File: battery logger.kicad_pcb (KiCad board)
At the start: 2 copper layers, 47 parts, among them CON501 BARREL_JACK, IC301 ATMEGA328-P, P201 CONN_01X02, P202 CONN_01X03, P301 CONN_02X03, P302 CONN_01X05, P501 CONN_01X02, P601 CONN_01X04, Q201 BUK9575, SW301 SW_PUSH, U201 TS922, U401 TLC2274, U501 LM2931ADT-5.0, U601 74HC14, X301 CRYSTAL 16MHZ

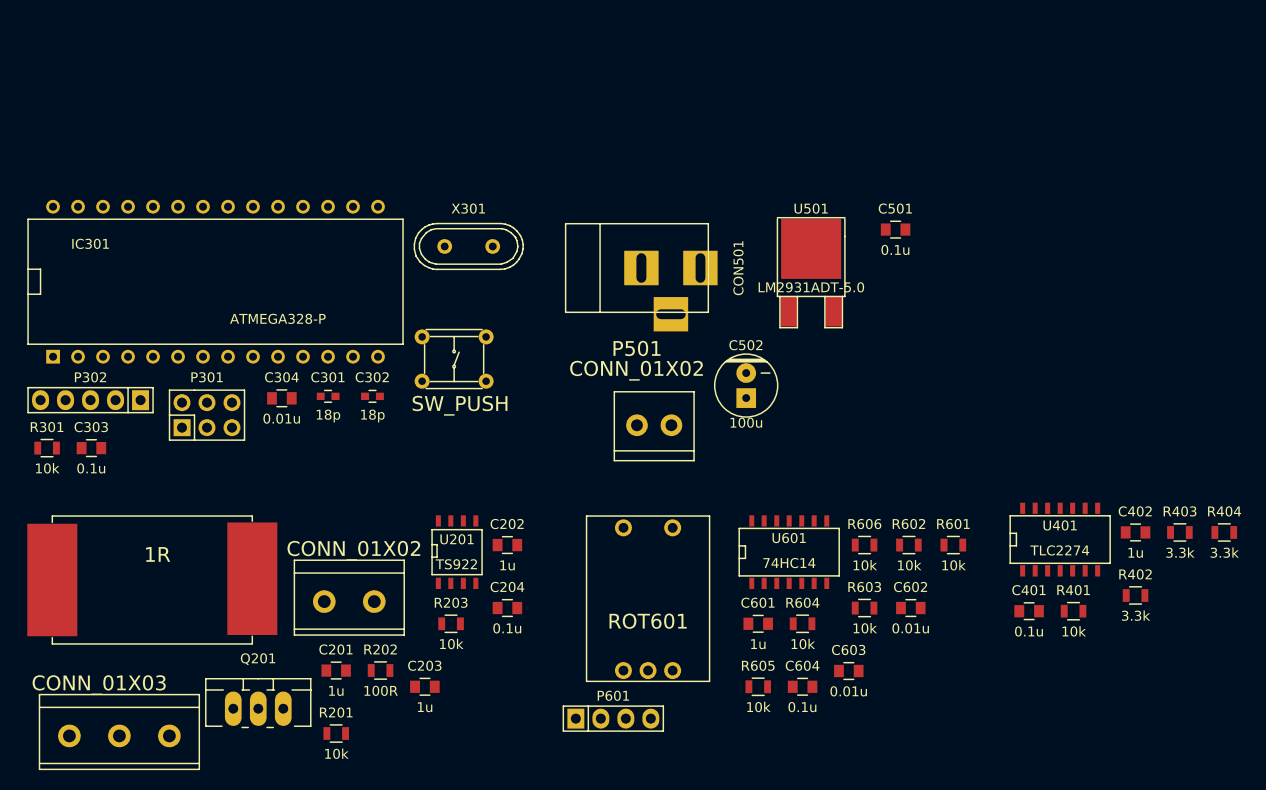
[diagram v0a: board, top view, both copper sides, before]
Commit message: initial part placemen
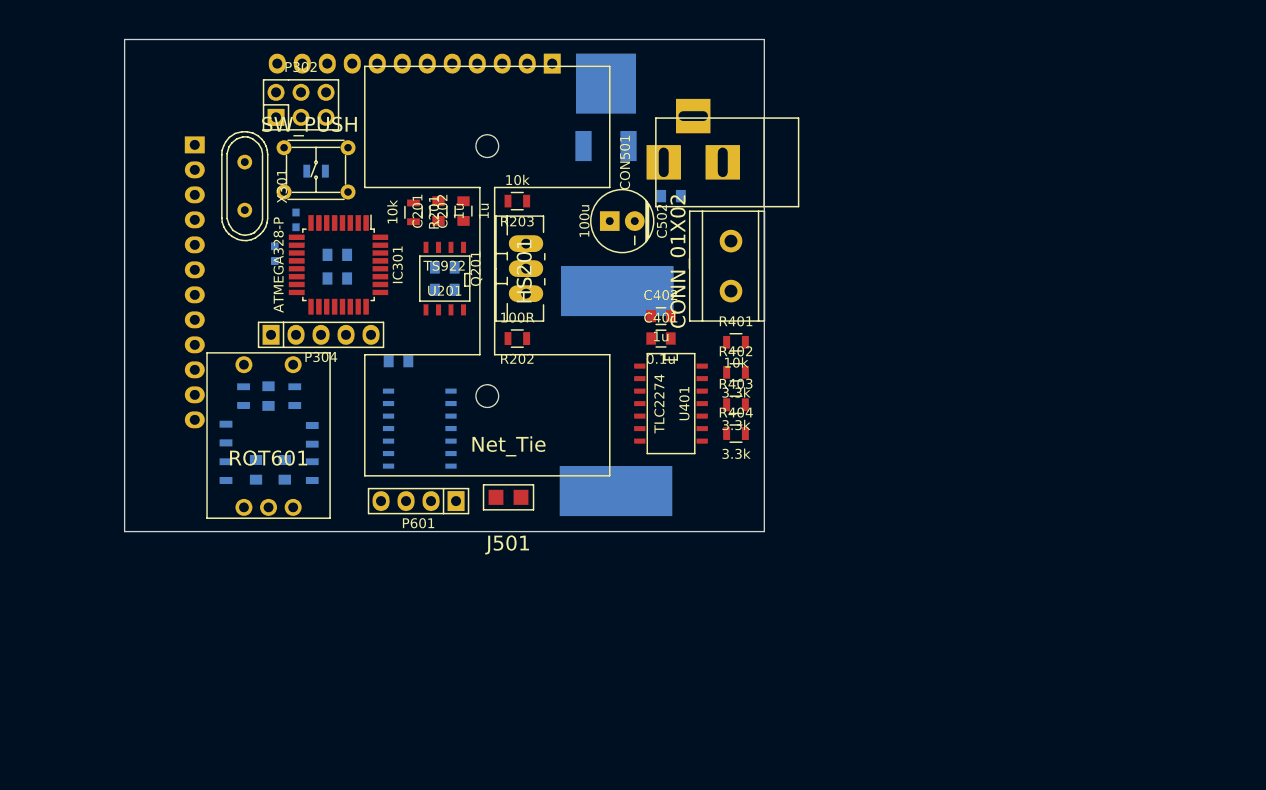
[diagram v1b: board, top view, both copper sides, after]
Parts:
- removed P202: CONN_01X03, battery logger:Terminal_Block_1x3_5.08mm
- removed P501: CONN_01X02, battery logger:Terminal_Block_1x2_3.5mm
- added HS201: HEATSINK, battery logger:FA-T220-38E, F.Cu at (196.8, 73.5)
- added J501: Net_Tie, battery logger:Net_Tie, F.Cu at (199.0, 96.5)
- added P303: CONN_01X12, Pin_Headers:Pin_Header_Straight_1x12, B.Cu at (189.5, 52.5)
- added P304: CONN_01X05, Socket_Strips:Socket_Strip_Straight_1x05, F.Cu at (180.0, 80.0)
- C203, C204, C301, C302, C303, C304, C501, C601, C602, C603, C604, R204, R301, R601, R602, R603, R604, R605, R606, U501, U601: moved to B.Cu
- IC301: footprint Sockets_DIP:DIP-28__600 -> Housings_QFP:TQFP-32_7x7mm_Pitch0.8mm
- P301: value CONN_02X03 -> CONN_01X12; footprint Pin_Headers:Pin_Header_Straight_2x03 -> Pin_Headers:Pin_Header_Straight_1x12; moved to B.Cu
- P302: value CONN_01X05 -> CONN_02X03; footprint Socket_Strips:Socket_Strip_Straight_1x05 -> Pin_Headers:Pin_Header_Straight_2x03
- moved R602 69.3 mm to (172.1, 86.2), turned to 270 degrees
- moved R601 68.6 mm to (177.3, 86.2), turned to 90 degrees
- moved R606 65.9 mm to (170.3, 90.0), turned to 270 degrees
- moved C602 65.1 mm to (176.3, 93.7), turned to 270 degrees
- moved R204 64.5 mm to (210.1, 75.6), turned to 270 degrees
- moved C603 63.6 mm to (173.4, 93.7), turned to 270 degrees
- moved R605 58.3 mm to (170.3, 93.9), turned to 90 degrees
- moved R603 57.8 mm to (179.1, 93.9), turned to 270 degrees
- moved C601 54.9 mm to (174.6, 86.2), turned to 90 degrees
- moved R201 53.5 mm to (189.4, 67.6), turned to 270 degrees
- moved R604 53.4 mm to (179.1, 90.2), turned to 270 degrees
- moved C402 53.0 mm to (214.5, 78.1)
- moved C604 52.7 mm to (187.8, 82.7)
- moved Q201 52.3 mm to (200.8, 73.3), turned to 90 degrees
- moved P201 52.0 mm to (221.6, 75.6), turned to 90 degrees
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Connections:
- C203 pad 1: /Current Sink/Enable -> /Current Sink/ENABLE
- C204 pad 1: /Current Sink/Enable -> /Current Sink/ENABLE
- IC301 pad 14: /Current Sink/Enable -> /Current Sink/ENABLE
- IC301 pad 4: /Encoder Interface/ENC_BTN -> /Encoder Interface/ENC_SW
- P301 pad 1: /uController/PB4 -> /uController/PC6
- P301 pad 2: VCC -> /uController/PD0
- P301 pad 3: /uController/CLK -> /uController/PD1
- P301 pad 4: /uController/DAT -> /Encoder Interface/ENC_SW
- P301 pad 5: /uController/PC6 -> /uController/PD3
- P301 pad 6: GNDD -> /Encoder Interface/ENC_A
- P302 pad 1: /uController/LAT -> /uController/PB4
- P302 pad 2: /uController/DAT -> VCC
- P302 pad 4: VCC -> /uController/DAT
- P302 pad 5: GNDD -> /uController/PC6
- P601 pad 3: /Encoder Interface/EMC_B -> /Encoder Interface/ENC_B
- U201 pad 8: /Current Sink/Enable -> /Current Sink/ENABLE
- U601 pad 12: /Encoder Interface/ENC_B -> /Encoder Interface/ENC_SW
- U601 pad 13: Net-(C603-Pad1) -> Net-(C601-Pad1)
- U601 pad 8: /Encoder Interface/ENC_BTN -> /Encoder Interface/ENC_B
- U601 pad 9: Net-(C601-Pad1) -> Net-(C603-Pad1)
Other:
- board outline added: 65 x 50 mm

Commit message: tweaking part layout
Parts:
- removed P601: CONN_01X04, Pin_Headers:Pin_Header_Straight_1x04
- added M3 screw hole: VAL**, battery logger:M3_screw_hole, F.Cu at (222.0, 52.6)
- added M3 screw hole: VAL**, battery logger:M3_screw_hole, F.Cu at (222.0, 97.4)
- added M3 screw hole: VAL**, battery logger:M3_screw_hole, F.Cu at (166.5, 97.4)
- added M3 screw hole: VAL**, battery logger:M3_screw_hole, F.Cu at (167.3, 52.6)
- added P305: CONN_01X01, Pin_Headers:Pin_Header_Straight_1x01, B.Cu at (197.4, 52.3)
- added P306: CONN_01X01, Pin_Headers:Pin_Header_Straight_1x01, B.Cu at (193.8, 52.3)
- added P307: CONN_01X01, Pin_Headers:Pin_Header_Straight_1x01, B.Cu at (190.2, 52.3)
- added P308: CONN_01X01, Pin_Headers:Pin_Header_Straight_1x01, B.Cu at (186.7, 52.3)
- added P309: CONN_01X01, Pin_Headers:Pin_Header_Straight_1x01, B.Cu at (189.1, 81.4)
- added P310: CONN_01X01, Pin_Headers:Pin_Header_Straight_1x01, B.Cu at (192.5, 81.4)
- added P311: CONN_01X01, Pin_Headers:Pin_Header_Straight_1x01, B.Cu at (196.1, 81.4)
- added P312: CONN_01X05, Socket_Strips:Socket_Strip_Straight_1x05, F.Cu at (171.8, 70.2)
- C401, C402: moved to B.Cu
- HS201: footprint battery logger:FA-T220-38E -> battery logger:FA-TO220-64E
- P301: value CONN_01X12 -> CONN_01X09; footprint Pin_Headers:Pin_Header_Straight_1x12 -> Pin_Headers:Pin_Header_Straight_1x09
- P303: value CONN_01X12 -> CONN_01X01; footprint Pin_Headers:Pin_Header_Straight_1x12 -> Pin_Headers:Pin_Header_Straight_1x01
- P304: value CONN_01X05 -> CONN_01X01; footprint Socket_Strips:Socket_Strip_Straight_1x05 -> Pin_Headers:Pin_Header_Straight_1x01; moved to B.Cu
- moved J501 39.8 mm to (198.9, 56.8)
- moved P304 34.7 mm to (200.9, 52.3), turned to 270 degrees
- moved P303 14.9 mm to (204.3, 52.3), turned to 90 degrees
- moved C402 9.65 mm to (209.3, 86.2), turned to 270 degrees
- moved P301 6.93 mm to (168.1, 67.8), turned to 180 degrees
- moved C401 6.48 mm to (211.7, 86.2), turned to 270 degrees
- moved X301 6.38 mm to (175.9, 70.1)
- moved R404 5.62 mm to (216.8, 91.8), turned to 180 degrees
- moved C302 5.03 mm to (180.2, 70.9), turned to 0 degrees
- moved U501 4.35 mm to (208.4, 65.2)
- moved P302 3.81 mm to (179.8, 53.3)
- moved C502 3.66 mm to (213.6, 70.5)
- moved R202 3.25 mm to (202.7, 82.0)
- moved R203 3.14 mm to (202.6, 68.1)
- moved C303 2.87 mm to (184.4, 73.7)
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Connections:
- P301 pad 4: /Encoder Interface/ENC_SW -> /uController/PD3
- P301 pad 5: /uController/PD3 -> /uController/PB6
- P301 pad 6: /Encoder Interface/ENC_A -> /uController/PB7
- P301 pad 7: /uController/PB6 -> /uController/PD6
- P301 pad 8: /uController/PB7 -> /uController/PD7
- P301 pad 9: /Encoder Interface/ENC_B -> /Current Sink/ENABLE
- P304 pad 1: /uController/LAT -> /Current Sink/I_SNS
- U601 pad 12: /Encoder Interface/ENC_SW -> /Encoder Interface/ENC_B
- U601 pad 13: Net-(C601-Pad1) -> Net-(C603-Pad1)
- U601 pad 8: /Encoder Interface/ENC_B -> /Encoder Interface/ENC_SW
- U601 pad 9: Net-(C603-Pad1) -> Net-(C601-Pad1)
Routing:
- net /Current Sink/BATT_V: track 0.00 -> 21.0 mm
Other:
- board size 65 x 50 mm -> 65 x 50.8 mm

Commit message: finished layout
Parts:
- removed C603: 0.01u, Capacitors_SMD:C_0805
- removed C604: 0.1u, Capacitors_SMD:C_0805
- removed CON501: BARREL_JACK, Connect:BARREL_JACK
- removed J501: Net_Tie, battery logger:Net_Tie
- removed the M3 screw hole at (222.0, 52.6)
- removed the M3 screw hole at (222.0, 97.4)
- removed the M3 screw hole at (166.5, 97.4)
- removed the M3 screw hole at (167.3, 52.6)
- removed P306, P307, P308, P309, P310, P311: CONN_01X01, Pin_Headers:Pin_Header_Straight_1x01
- removed P312: CONN_01X05, Socket_Strips:Socket_Strip_Straight_1x05
- removed R601, R602, R603, R604, R605, R606: 10k, Resistors_SMD:R_0805
- removed ROT601: Rotary_Encoder, battery logger:PEC11R
- added C503: 0.01u, Capacitors_SMD:C_0805, B.Cu at (173.4, 94.4)
- added C504: 0.1u, Capacitors_SMD:C_0805, B.Cu at (185.3, 80.5)
- added CON601: BARREL_JACK, Connect:BARREL_JACK, F.Cu at (221.5, 61.3)
- added D201: DIODESCH, Diodes_SMD:Diode-SMB_Standard, F.Cu at (212.4, 76.1)
- added F601: FUSE, battery logger:PTC_1206, B.Cu at (214.6, 65.9)
- added J601: Net_Tie, battery logger:Net_Tie2, B.Cu at (190.8, 59.1)
- added M3 screw hole: VAL**, battery logger:M3_screw_hole, F.Cu at (222.0, 97.4)
- added M3 screw hole: VAL**, battery logger:M3_screw_hole, F.Cu at (183.8, 97.3)
- added M3 screw hole: VAL**, battery logger:M3_screw_hole, F.Cu at (171.1, 52.7)
- added M3 screw hole: VAL**, battery logger:M3_screw_hole, F.Cu at (221.9, 52.7)
- added P202: CONN_02X02, Pin_Headers:Pin_Header_Straight_2x02, F.Cu at (219.7, 79.5)
- added P601: CONN_01X02, Pin_Headers:Pin_Header_Straight_1x02, F.Cu at (214.9, 52.2)
- added R205: 10k, Resistors_SMD:R_0805, F.Cu at (196.1, 69.2)
- added R501: 10k, Resistors_SMD:R_0805, B.Cu at (177.6, 86.9)
- added R502: 10k, Resistors_SMD:R_0805, B.Cu at (171.8, 86.9)
- added R503: 10k, Resistors_SMD:R_0805, B.Cu at (179.4, 94.5)
- added R504: 10k, Resistors_SMD:R_0805, B.Cu at (179.4, 90.7)
- added R505: 10k, Resistors_SMD:R_0805, B.Cu at (170.3, 94.5)
- added R506: 10k, Resistors_SMD:R_0805, B.Cu at (170.3, 90.6)
- added ROT501: Rotary_Encoder, battery logger:PEC11R, F.Cu at (174.7, 90.7)
- added TH201: THERMISTOR, battery logger:SolderWirePad_2x_0-8mmDrill, F.Cu at (202.5, 68.0)
- C501: value 0.1u -> 1u
- C502: value 100u -> 0.01u; footprint battery logger:Capacitor6.4x6RM2.5 -> Capacitors_SMD:C_0805; moved to B.Cu
- C601: value 1u -> 0.1u
- C602: value 0.01u -> 100u; footprint Capacitors_SMD:C_0805 -> battery logger:Capacitor6.4x6RM2.5; moved to F.Cu
- IC301: value ATMEGA328-P -> ATMEGA328P-A
- P301: value CONN_01X09 -> CONN_02X03; footprint Pin_Headers:Pin_Header_Straight_1x09 -> Pin_Headers:Pin_Header_Straight_2x03; moved to F.Cu
- P303, P305: value CONN_01X01 -> CONN_01X07; footprint Pin_Headers:Pin_Header_Straight_1x01 -> Pin_Headers:Pin_Header_Straight_1x07; moved to F.Cu
- P304: value CONN_01X01 -> CONN_02X02; footprint Pin_Headers:Pin_Header_Straight_1x01 -> Pin_Headers:Pin_Header_Straight_2x02; moved to F.Cu
- R204: footprint battery logger:FA -> battery logger:8035_J-Lead
- SW301: value SW_PUSH -> SW_PUSH_4_PIN
- U501: value LM2931ADT-5.0 -> 74HC14; footprint SMD_Packages:DPAK-2 -> SMD_Packages:SOIC-14_N
- U601: value 74HC14 -> LM2931ADT-5.0; footprint SMD_Packages:SOIC-14_N -> SMD_Packages:DPAK-2
- moved P305 46.7 mm to (204.4, 98.5), turned to 270 degrees
- moved C501 44.8 mm to (174.8, 86.9), turned to 90 degrees
- moved C502 44.2 mm to (176.5, 94.4)
- moved C602 42.0 mm to (212.3, 70.1)
- moved C601 39.3 mm to (209.8, 66.0), turned to 180 degrees
- moved P304 34.9 mm to (170.6, 69.5), turned to 90 degrees
- moved U601 34.6 mm to (208.4, 61.7), turned to 180 degrees
- moved U501 31.0 mm to (188.3, 88.7), turned to 270 degrees
- moved P302 24.2 mm to (171.9, 76.2), turned to 270 degrees
- moved P303 17.5 mm to (186.9, 52.2)
- moved P301 16.3 mm to (177.8, 54.7), turned to 90 degrees
- moved R201 13.3 mm to (187.1, 81.2), turned to 0 degrees
- moved C201 12.6 mm to (195.0, 81.3), turned to 270 degrees
- moved C202 12.3 mm to (190.5, 79.3), turned to 270 degrees
- moved R403 11.5 mm to (214.9, 97.3)
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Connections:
- C201 pad 2: GND -> GNDD
- C501 pad 2: GND -> GNDD
- C502 pad 1: VCC -> Net-(C502-Pad1)
- C502 pad 2: GND -> GNDD
- C602 pad 1: Net-(C602-Pad1) -> VCC
- IC301 pad 1: /uController/PC6 -> /Current Sink/ENABLE
- IC301 pad 10: /uController/PB7 -> /uController/PD6
- IC301 pad 11: /Encoder Interface/ENC_B -> /uController/PD7
- IC301 pad 12: /uController/PD6 -> /uController/PB0
- IC301 pad 13: /uController/PD7 -> /Current Sink/V_SET
- IC301 pad 14: /Current Sink/ENABLE -> /uController/LAT
- IC301 pad 15: /Current Sink/V_SET -> /uController/DAT
- IC301 pad 16: /uController/LAT -> /uController/MISO
- IC301 pad 17: /uController/DAT -> /uController/CLK
- IC301 pad 18: /uController/PB4 -> VCC
- IC301 pad 19: /uController/CLK -> /uController/ADC6
- IC301 pad 2: /uController/PD0 -> /Encoder Interface/ENC_A
- IC301 pad 20: VCC -> /uController/AREF
- IC301 pad 21: /uController/AREF -> GNDD
- IC301 pad 22: GNDD -> /uController/ADC7
- IC301 pad 23: /Input Voltage Range Switch/V_SNS1 -> /Input Voltage Range Switch/V_SNS4
- IC301 pad 24: /Input Voltage Range Switch/V_SNS2 -> /Input Voltage Range Switch/V_SNS3
- IC301 pad 25: /Input Voltage Range Switch/V_SNS3 -> /Input Voltage Range Switch/V_SNS2
- IC301 pad 26: /Input Voltage Range Switch/V_SNS4 -> /Input Voltage Range Switch/V_SNS1
- IC301 pad 28: /uController/PC5 -> /Current Sink/AUX
- IC301 pad 29: (no net) -> /uController/PC6
- IC301 pad 3: /uController/PD1 -> GNDD
- IC301 pad 30: (no net) -> /uController/PD0
- IC301 pad 31: (no net) -> /uController/PD1
- IC301 pad 32: (no net) -> /Encoder Interface/ENC_SW
- IC301 pad 4: /Encoder Interface/ENC_SW -> VCC
- IC301 pad 5: /uController/PD3 -> GNDD
- IC301 pad 6: /Encoder Interface/ENC_A -> VCC
- IC301 pad 7: VCC -> /uController/PB6
- IC301 pad 8: GNDD -> /uController/PB7
- IC301 pad 9: /uController/PB6 -> /Encoder Interface/ENC_B
- P201 pad 1: /Current Sink/BATT_V -> Net-(D201-Pad1)
- P301 pad 1: /uController/PC6 -> /uController/MISO
- P301 pad 2: /uController/PD0 -> VCC
- P301 pad 3: /uController/PD1 -> /uController/CLK
- P301 pad 4: /uController/PD3 -> /uController/DAT
- P301 pad 5: /uController/PB6 -> /uController/PC6
- P301 pad 6: /uController/PB7 -> GNDD
- P302 pad 1: /uController/PB4 -> VCC
- P302 pad 2: VCC -> /uController/LAT
- P302 pad 3: /uController/CLK -> GNDD
- P302 pad 5: /uController/PC6 -> GNDD
- P302 pad 6: GNDD -> /uController/CLK
- P303 pad 1: /uController/PC5 -> /uController/PD1
- P304 pad 1: /Current Sink/I_SNS -> /Current Sink/V_SET
- P305 pad 1: /Input Voltage Range Switch/V_SNS4 -> /Input Voltage Range Switch/V_SNS1
- Q201 pad D: /Current Sink/BATT_V -> Net-(D201-Pad2)
- SW301 pad 1: GND -> /uController/PC6
- SW301 pad 2: /uController/PC6 -> GNDD
- SW301 pad 3: (no net) -> GNDD
- SW301 pad 4: (no net) -> /uController/PC6
- U201 pad 5: (no net) -> Net-(R205-Pad2)
- U201 pad 6: (no net) -> /Current Sink/AUX
- U201 pad 7: (no net) -> /Current Sink/AUX
- U401 pad 1: /Input Voltage Range Switch/V_SNS1 -> /Input Voltage Range Switch/V_SNS4
- U401 pad 10: Net-(R402-Pad2) -> Net-(R401-Pad2)
- U401 pad 12: Net-(R403-Pad2) -> /Current Sink/BATT_V
- U401 pad 13: /Input Voltage Range Switch/V_SNS4 -> /Input Voltage Range Switch/V_SNS1
- U401 pad 14: /Input Voltage Range Switch/V_SNS4 -> /Input Voltage Range Switch/V_SNS1
- U401 pad 2: /Input Voltage Range Switch/V_SNS1 -> /Input Voltage Range Switch/V_SNS4
- U401 pad 3: /Current Sink/BATT_V -> Net-(R403-Pad2)
- U401 pad 5: Net-(R401-Pad2) -> Net-(R402-Pad2)
- U401 pad 6: /Input Voltage Range Switch/V_SNS2 -> /Input Voltage Range Switch/V_SNS3
- U401 pad 7: /Input Voltage Range Switch/V_SNS2 -> /Input Voltage Range Switch/V_SNS3
- U401 pad 8: /Input Voltage Range Switch/V_SNS3 -> /Input Voltage Range Switch/V_SNS2
- U401 pad 9: /Input Voltage Range Switch/V_SNS3 -> /Input Voltage Range Switch/V_SNS2
- U501 pad 1: Net-(C501-Pad1) -> Net-(U501-Pad1)
- U501 pad 2: GND -> Net-(U501-Pad2)
- U501 pad 3: VCC -> Net-(U501-Pad3)
- U601 pad 1: Net-(U601-Pad1) -> Net-(C601-Pad1)
- U601 pad 2: Net-(U601-Pad2) -> GND
- U601 pad 3: Net-(U601-Pad3) -> VCC
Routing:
- net VCC: track 0.00 -> 241.8 mm, vias 0 -> 8
- net /Input Voltage Range Switch/V_SNS2: track 0.00 -> 64.6 mm, vias 0 -> 4
- net /Input Voltage Range Switch/V_SNS3: track 0.00 -> 64.5 mm, vias 0 -> 4
- net /Input Voltage Range Switch/V_SNS1: track 0.00 -> 58.5 mm, vias 0 -> 4
- net /Input Voltage Range Switch/V_SNS4: track 0.00 -> 52.7 mm, vias 0 -> 2
- net /Encoder Interface/ENC_B: track 0.00 -> 43.0 mm, vias 0 -> 3
- net /Encoder Interface/ENC_A: track 0.00 -> 42.0 mm, vias 0 -> 2
- net /uController/PC6: track 0.00 -> 40.8 mm, vias 0 -> 2
- net /Encoder Interface/ENC_SW: track 0.00 -> 40.5 mm, vias 0 -> 2
- net /Current Sink/ENABLE: track 0.00 -> 35.0 mm, vias 0 -> 2
- net /uController/DAT: track 0.00 -> 33.5 mm, vias 0 -> 1
- net /uController/CLK: track 0.00 -> 33.1 mm, vias 0 -> 1
- net /Current Sink/I_SNS: track 0.00 -> 26.0 mm
- net /uController/PD1: track 0.00 -> 25.2 mm
- net /Current Sink/V_SET: track 0.00 -> 24.6 mm, vias 0 -> 2
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- added copper zone on B.Cu, net GND
- added copper zone on B.Cu, net GNDD
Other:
- board size 65 x 50.8 mm -> 57 x 50.8 mm
- net class Analog Signal added: clearance 0.1524, trace_width 0.1524, via_dia 0.6858, via_drill 0.3302
- net class Digital Signal added: clearance 0.1524, trace_width 0.1524, via_dia 0.6858, via_drill 0.3302
- net class Power added: clearance 0.254, trace_width 0.381, via_dia 0.889, via_drill 0.635
- rule trace_min: 0.254 -> 0.1524
- rule via_min_drill: 0.508 -> 0.3302
- rule via_min_size: 0.889 -> 0.6858

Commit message: minor tweaks
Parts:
- P202: value CONN_02X02 -> CONN_01X02; footprint Pin_Headers:Pin_Header_Straight_2x02 -> Pin_Headers:Pin_Header_Straight_1x02
- moved P202 0.57 mm to (219.6, 80.1), turned to 90 degrees
- moved CON601 0.45 mm to (221.1, 61.5)
- moved R301 0.28 mm to (173.9, 60.5)
- moved SW301 0.26 mm to (172.6, 60.7)
- moved P301 0.23 mm to (177.6, 54.7)
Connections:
- P202 pad 2: Net-(P202-Pad2) -> /Current Sink/BATT_V
- P303 pad 4: GND -> /Current Sink/AUX
- P303 pad 5: GND -> VCC
- P303 pad 7: VCC -> GND
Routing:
- net /Current Sink/AUX: track 7.25 -> 27.3 mm
- net Net-(R505-Pad1): track 5.92 -> 4.78 mm
- net /uController/PC6: track 40.8 -> 39.9 mm
- net /Voltage Regulator/Vs: track 14.8 -> 15.4 mm
- net /uController/MISO: track 24.3 -> 23.7 mm
- net /Current Sink/BATT_V: track 11.1 -> 10.6 mm

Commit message: generated gerber files
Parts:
- SW301: value SW_PUSH_4_PIN -> Reset SW
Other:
- board text added: "GND"
- board text added: "GNDD"
- board text added: "ICSP"
- board text added: "PB0"
- board text added: "PB1"
- board text added: "PB2"
- board text added: "PB3"
- board text added: "PB5"
- board text added: "PB6"
- board text added: "PB7"
- board text added: "PC0"
- board text added: "PC1"
- board text added: "PC2"
- board text added: "PC3"
- board text added: "PD0"
- board text added: "PD1"
- board text added: "PD2"
- board text added: "PD3"
- board text added: "PD4"
- board text added: "PD5"
- board text added: "PD6"
- board text added: "PD7"
- board text added: "V sns"
- board text added: "V+"
- board text added: "VCC"

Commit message: BOM update
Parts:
- moved C504 0.89 mm to (185.2, 81.4)
- moved R506 0.20 mm to (170.3, 90.8)
- moved R504 0.15 mm to (179.3, 90.8)
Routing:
- net /uController/PC6: track 39.9 -> 55.7 mm
- net /uController/CLK: track 33.1 -> 37.9 mm, vias 1 -> 0
- net Net-(C502-Pad1): track 13.3 -> 17.5 mm, vias 2 -> 3
- net /uController/DAT: track 33.4 -> 37.1 mm, vias 1 -> 2
- net Net-(C503-Pad1): track 18.9 -> 22.3 mm, vias 2 -> 3
- net /Current Sink/V_SET: track 24.6 -> 27.3 mm
- net Net-(C501-Pad1): track 14.8 -> 16.4 mm, vias 2 -> 4
- net VCC: track 241.7 -> 240.7 mm, vias 8 -> 9
- net /uController/MISO: track 23.7 -> 23.6 mm, vias 1 -> 2

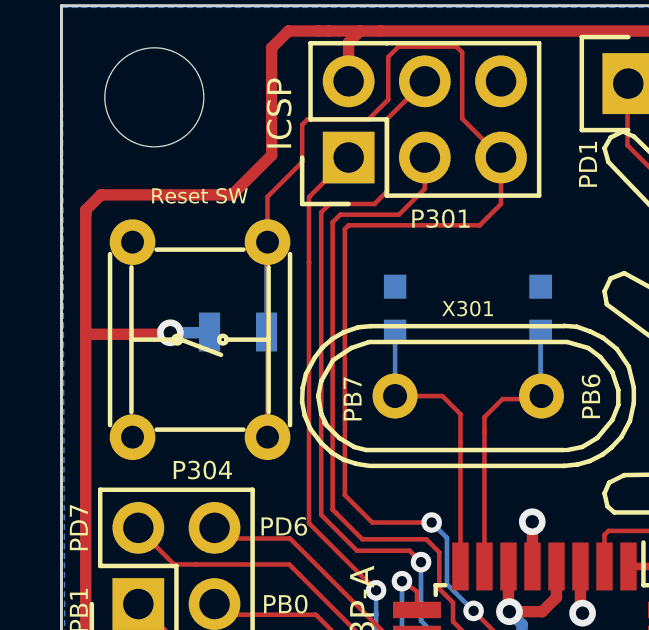
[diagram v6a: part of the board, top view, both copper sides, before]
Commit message: schematic correction
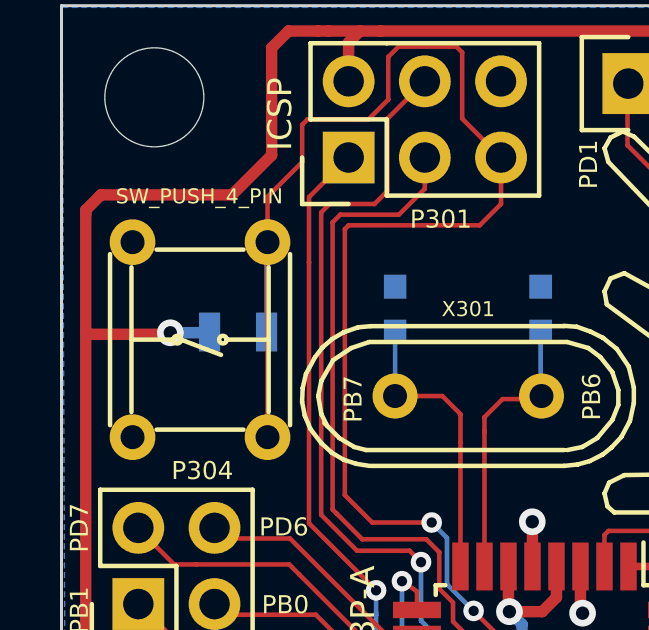
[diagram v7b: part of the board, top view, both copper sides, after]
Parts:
- R501, R503, R505: value 10k -> 3.3k
- SW301: value Reset SW -> SW_PUSH_4_PIN
